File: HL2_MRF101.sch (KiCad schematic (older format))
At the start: 213 parts, among them J1 Antenna, J10 DB1, J2 HL2, J3 RF3, J4 RF1, J5 RCJ-041, J6 50VDC, J7 12V, J8 Fan, J9 HL2_12V, K1 EC2-3NU, K10 EC2-3NU, K11 EC2-3NU, K12 EC2-3NU, K13 EC2-3NU, K2 EC2-3NU, K3 EC2-3NU, K4 EC2-3NU, K5 EC2-3NU, K6 EC2-3NU, K7 EC2-3NU, K8 EC2-3NU, K9 EC2-3NU, Q1 MRF101AN, Q2 2N7002, Q3 IRLML6402, Q4 DTC144E, T1 Coupler, T2 Coupler, T3 744851330, U1 MCP6282E/MS, U2 MAX11613, U3 MCP23008, U4 ULN2003, U5 LM35-NEB, U6 MCP4561, U7 INA193

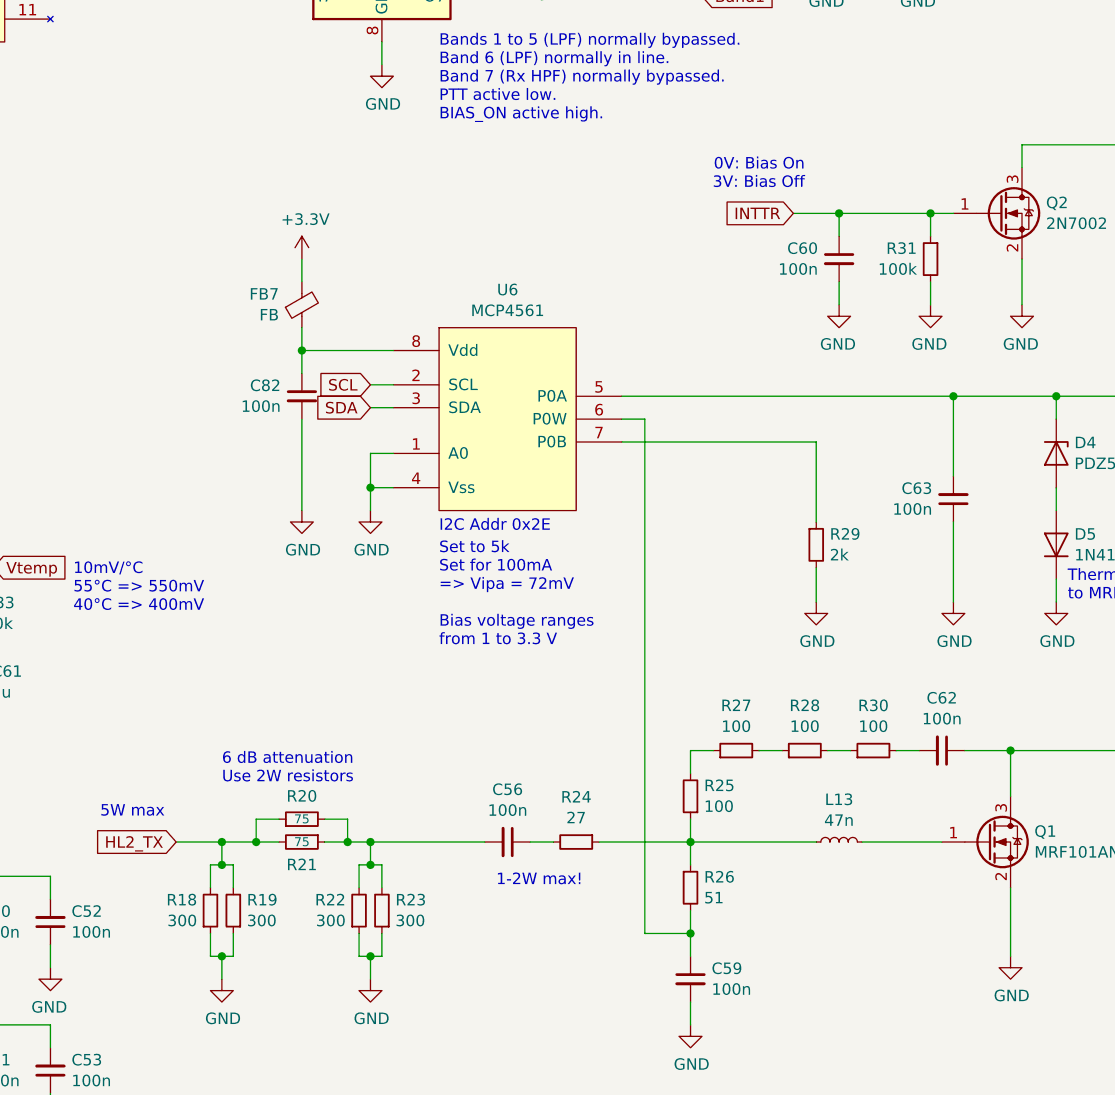
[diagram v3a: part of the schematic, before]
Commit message: Reworked bias circuit
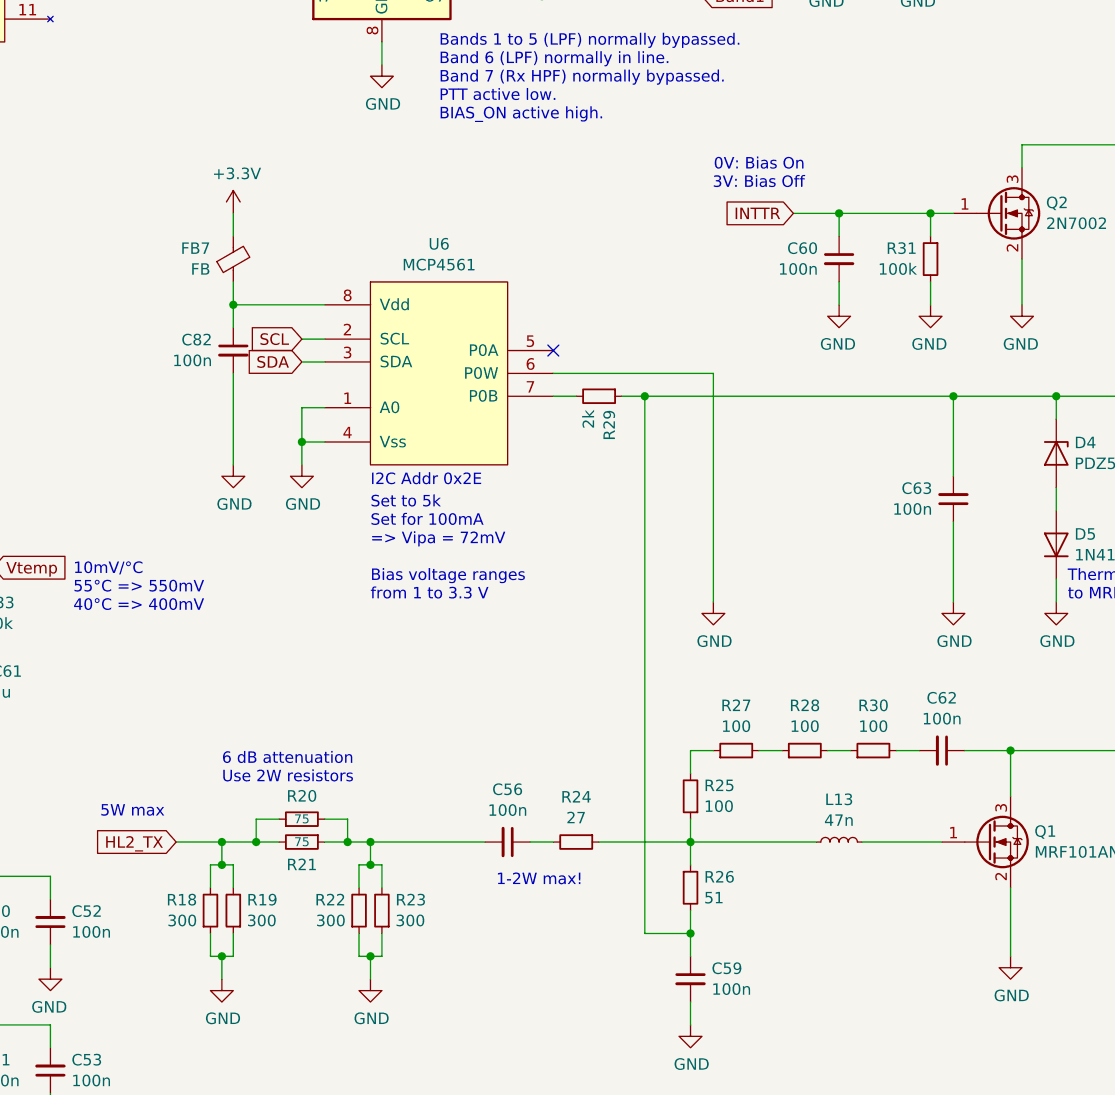
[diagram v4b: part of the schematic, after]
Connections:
- net GND: now also U6.6 (P0W); no longer R29.2
- net at C63.2, D4.1 (K), Q2.3 (D)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: now also C59.1, R26.2, R29.1; no longer U6.5 (P0A)
- net at U6.7 (P0B): now also R29.2; no longer R29.1
- no-connect marks 9 -> 10
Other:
- moved on the sheet: C82, FB7, R29, U6
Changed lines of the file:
@@
 Text Notes 12600 4850 0    50   ~ 0
 Thermally coupled\nto MRF-101
-Connection ~ 12100 3950
 $Comp
 L HL2_MRF101-rescue:R_Small-Device R32
@@
 Wire Wire Line
 	13900 4650 14000 4650
-Text Notes 9850 5050 0    50   ~ 0
+Text Notes 9550 4850 0    50   ~ 0
 Set to 5k\nSet for 100mA\n=> Vipa = 72mV\n\nBias voltage ranges\nfrom 1 to 3.3 V
 Text Notes 10100 6100 0    50   ~ 0
@@
 L HL2-MRF101:MCP4561 U6
 U 1 1 6200A830
-P 10150 4050
-F 0 "U6" H 10150 4615 50  0000 C CNN
-F 1 "MCP4561" H 10150 4524 50  0000 C CNN
-F 2 "Package_SO:MSOP-8_3x3mm_P0.65mm" H 9950 5700 50  0001 C CNN
-F 3 "" H 9950 5700 50  0001 C CNN
-	1    10150 4050
+P 9850 3850
+F 0 "U6" H 9850 4415 50  0000 C CNN
+F 1 "MCP4561" H 9850 4324 50  0000 C CNN
+F 2 "Package_SO:MSOP-8_3x3mm_P0.65mm" H 9650 5500 50  0001 C CNN
+F 3 "" H 9650 5500 50  0001 C CNN
+	1    9850 3850
 	1    0    0    -1
 $EndComp
-Wire Wire Line
-	10650 4050 10750 4050
-Wire Wire Line
-	10650 3950 12100 3950
-Text GLabel 9550 3900 0    50   Input ~ 0
+Text GLabel 9250 3700 0    50   Input ~ 0
 SCL
-Text GLabel 9550 4000 0    50   Input ~ 0
+Text GLabel 9250 3800 0    50   Input ~ 0
 SDA
 Wire Wire Line
-	9650 4000 9550 4000
+	9350 3800 9250 3800
 Wire Wire Line
-	9650 3900 9550 3900
+	9350 3700 9250 3700
 Wire Wire Line
-	9250 3750 9650 3750
+	8950 3550 9350 3550
 $Comp
 L HL2_MRF101-rescue:C_Small-Device C82
 U 1 1 6244D31F
-P 9250 3950
-F 0 "C82" H 9342 3996 50  0000 L CNN
-F 1 "100n" H 9342 3905 50  0000 L CNN
-F 2 "Capacitor_SMD:C_0805_2012Metric" H 9250 3950 50  0001 C CNN
-F 3 "~" H 9250 3950 50  0001 C CNN
-	1    9250 3950
+P 8950 3750
+F 0 "C82" H 9042 3796 50  0000 L CNN
+F 1 "100n" H 9042 3705 50  0000 L CNN
+F 2 "Capacitor_SMD:C_0805_2012Metric" H 8950 3750 50  0001 C CNN
+F 3 "~" H 8950 3750 50  0001 C CNN
+	1    8950 3750
 	-1   0    0    -1
 $EndComp
 Wire Wire Line
-	9250 3750 9250 3850
+	8950 3550 8950 3650
 $Comp
 L power:+3.3V #PWR0104
 U 1 1 624EB2A7
-P 9250 3350
-F 0 "#PWR0104" H 9250 3200 50  0001 C CNN
-F 1 "+3.3V" H 9265 3523 50  0000 C CNN
-F 2 "" H 9250 3350 50  0001 C CNN
-F 3 "" H 9250 3350 50  0001 C CNN
-	1    9250 3350
+P 8950 3150
+F 0 "#PWR0104" H 8950 3000 50  0001 C CNN
+F 1 "+3.3V" H 8965 3323 50  0000 C CNN
+F 2 "" H 8950 3150 50  0001 C CNN
+F 3 "" H 8950 3150 50  0001 C CNN
+	1    8950 3150
 	1    0    0    -1
 $EndComp
@@
 L HL2_MRF101-rescue:Ferrite_Bead_Small-device FB7
 U 1 1 624EB2B1
-P 9250 3550
-F 0 "FB7" H 9150 3504 50  0000 R CNN
-F 1 "FB" H 9150 3595 50  0000 R CNN
-F 2 "Inductor_SMD:L_0805_2012Metric" V 9180 3550 50  0001 C CNN
-F 3 "~" H 9250 3550 50  0001 C CNN
-	1    9250 3550
+P 8950 3350
+F 0 "FB7" H 8850 3304 50  0000 R CNN
+F 1 "FB" H 8850 3395 50  0000 R CNN
+F 2 "Inductor_SMD:L_0805_2012Metric" V 8880 3350 50  0001 C CNN
+F 3 "~" H 8950 3350 50  0001 C CNN
+	1    8950 3350
 	1    0    0    1
 $EndComp
 Wire Wire Line
-	9250 3350 9250 3450
+	8950 3150 8950 3250
 Wire Wire Line
-	9250 3650 9250 3750
+	8950 3450 8950 3550
 $Comp
 L power:GND #PWR0112
 U 1 1 62627FA1
-P 9550 4450
-F 0 "#PWR0112" H 9550 4200 50  0001 C CNN
-F 1 "GND" H 9555 4277 50  0000 C CNN
-F 2 "" H 9550 4450 50  0001 C CNN
-F 3 "" H 9550 4450 50  0001 C CNN
-	1    9550 4450
+P 9250 4250
+F 0 "#PWR0112" H 9250 4000 50  0001 C CNN
+F 1 "GND" H 9255 4077 50  0000 C CNN
+F 2 "" H 9250 4250 50  0001 C CNN
+F 3 "" H 9250 4250 50  0001 C CNN
+	1    9250 4250
 	1    0    0    -1
 $EndComp
 Wire Wire Line
-	9650 4350 9550 4350
+	9350 4150 9250 4150
 Wire Wire Line
-	9550 4350 9550 4450
+	9250 4150 9250 4250
 $Comp
 L power:GND #PWR0111
 U 1 1 626C7205
-P 9250 4450
-F 0 "#PWR0111" H 9250 4200 50  0001 C CNN
-F 1 "GND" H 9255 4277 50  0000 C CNN
-F 2 "" H 9250 4450 50  0001 C CNN
-F 3 "" H 9250 4450 50  0001 C CNN
-	1    9250 4450
+P 8950 4250
+F 0 "#PWR0111" H 8950 4000 50  0001 C CNN
+F 1 "GND" H 8955 4077 50  0000 C CNN
+F 2 "" H 8950 4250 50  0001 C CNN
+F 3 "" H 8950 4250 50  0001 C CNN
+	1    8950 4250
 	1    0    0    -1
 $EndComp
 Wire Wire Line
-	9250 4050 9250 4450
-Text Notes 9850 4550 0    50   ~ 0
+	8950 3850 8950 4250
+Text Notes 9550 4350 0    50   ~ 0
 I2C Addr 0x2E
 Wire Wire Line
-	9650 4200 9550 4200
+	9350 4000 9250 4000
 Wire Wire Line
-	9550 4200 9550 4350
-Connection ~ 9550 4350
-Connection ~ 9250 3750
+	9250 4000 9250 4150
+Connection ~ 9250 4150
+Connection ~ 8950 3550
 Text Notes 14450 3550 0    50   ~ 0
 4A => 144mV
@@
 Wire Wire Line
 	5100 10550 5200 10550
-Wire Wire Line
-	10750 4050 10750 6300
-Wire Wire Line
-	10650 4150 11500 4150
-Wire Wire Line
-	11500 4150 11500 4500
-Wire Wire Line
-	11500 4700 11500 4850
-$Comp
-L power:GND #PWR081
-U 1 1 5E0C0657
-P 11500 4850
-F 0 "#PWR081" H 11500 4600 50  0001 C CNN
-F 1 "GND" H 11505 4677 50  0000 C CNN
-F 2 "" H 11500 4850 50  0001 C CNN
-F 3 "" H 11500 4850 50  0001 C CNN
-	1    11500 4850
-	1    0    0    -1
-$EndComp
 $Comp
 L HL2_MRF101-rescue:R_Small-Device R29
 U 1 1 5E0BF37A
-P 11500 4600
-F 0 "R29" H 11559 4646 50  0000 L CNN
-F 1 "2k" H 11559 4555 50  0000 L CNN
-F 2 "Resistor_SMD:R_0805_2012Metric" H 11500 4600 50  0001 C CNN
-F 3 "~" H 11500 4600 50  0001 C CNN
-	1    11500 4600
-	1    0    0    -1
+P 10550 3950
+F 0 "R29" H 10609 3996 50  0000 L CNN
+F 1 "2k" H 10609 3905 50  0000 L CNN
+F 2 "Resistor_SMD:R_0805_2012Metric" H 10550 3950 50  0001 C CNN
+F 3 "~" H 10550 3950 50  0001 C CNN
+	1    10550 3950
+	0    1    1    0
 $EndComp
 Text GLabel 1000 8950 2    50   Input ~ 0
@@
 Wire Wire Line
 	1750 10350 1850 10350
+NoConn ~ 10350 3750
+Wire Wire Line
+	10350 3950 10450 3950
+Wire Wire Line
+	10750 6300 10750 3950
+Wire Wire Line
+	10750 3950 10650 3950
+Wire Wire Line
+	10750 3950 12100 3950
+Connection ~ 10750 3950
+Connection ~ 12100 3950
+Wire Wire Line
+	10350 3850 11050 3850
+Wire Wire Line
+	11050 3850 11050 4850
+$Comp
+L power:GND #PWR?
+U 1 1 63E68A3C
+P 11050 4850
+F 0 "#PWR?" H 11050 4600 50  0001 C CNN
+F 1 "GND" H 11055 4677 50  0000 C CNN
+F 2 "" H 11050 4850 50  0001 C CNN
+F 3 "" H 11050 4850 50  0001 C CNN
+	1    11050 4850
+	1    0    0    -1
+$EndComp
 $EndSCHEMATC
